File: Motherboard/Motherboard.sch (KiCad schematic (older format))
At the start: 163 parts, among them J1 Jack-DC_18v, J2 65SIB_Connector, J3 DB9_Header, J4 GPIO_Connector, J5 Expansion_Connector, J6 Expansion_Connector, J7 Expansion_Connector, J8 Expansion_Connector, P1 POWER TERMINAL, Q1 2N3055, Q2 TIC106, SW1 SW_DPDT, SW2 FUSE RESET, SW3 PROCESSOR RESET, U1 LM7812_TO220, U13 LM386, U14 LM7912_TO220, U4 LM7805_TO220, X1 ACO-8MHz

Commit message: Completed schematic for 2.3...
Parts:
- added ROM_NOR1, ROM_NOR2 (x3): 74HCT04, symbol 74xx:74HCT04
- gave numbers to parts that had none: 21
- renumbered RAM_NAND to RAM_NAND2, RAM_NOR to RAM_NOR1
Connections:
- net A14: now also ROM_NOR1.9, ROM_NOR2.9, ROM_NOR2.9, ROM_NOR2.9; no longer ROM1_NAND1.10, ROM2_NAND1.10, ROM3_NAND1.10, ROM4_NAND1.10
- net ROM2_EN: now also ROM_NOR1.1, ROM_NOR2.1; no longer ROM_NOR1.9, ROM_NOR2.9
- net ROM3_EN: now also ROM_NOR2.9; no longer ROM_NOR2.1
- net ROM4_EN: now also ROM_NOR3.1; no longer ROM_NOR3.9
- net at ROM2_NAND1.5: now also ROM_NOR1.6; no longer ROM_NOR1.12
- net at ROM2_NAND1.6: now also ROM_NOR1.3; no longer ROM_NOR1.11
- net at ROM2_NAND1.8: now also ROM_NOR1.5; no longer ROM_NOR1.13
- net at ROM2_NAND1.1: now also ROM_NOR1.4; no longer ROM_NOR1.10
- net at ROM2_NAND1.2: now also ROM_NOR1.2; no longer ROM_NOR1.8
- net at ROM2_NAND2.5: now also ROM_NOR2.6; no longer ROM_NOR2.12
- net at ROM2_NAND2.6: now also ROM_NOR2.3; no longer ROM_NOR2.11
- net at ROM2_NAND2.8: now also ROM_NOR2.5; no longer ROM_NOR2.13
- net at ROM2_NAND2.1: now also ROM_NOR2.4; no longer ROM_NOR2.10
- net at ROM2_NAND2.2: now also ROM_NOR2.2; no longer ROM_NOR2.8
- net at ROM3_NAND2.5: now also ROM_NOR2.12; no longer ROM_NOR2.6
- net at ROM3_NAND2.6: now also ROM_NOR2.11; no longer ROM_NOR2.3
- net at ROM3_NAND2.8: now also ROM_NOR2.13; no longer ROM_NOR2.5
- net at ROM3_NAND2.1: now also ROM_NOR2.10; no longer ROM_NOR2.4
- net at ROM3_NAND2.2: now also ROM_NOR2.8; no longer ROM_NOR2.2
- net at ROM4_NAND2.5: now also ROM_NOR3.6; no longer ROM_NOR3.12
- net at ROM4_NAND2.6: now also ROM_NOR3.3; no longer ROM_NOR3.11
- net at ROM4_NAND2.8: now also ROM_NOR3.5; no longer ROM_NOR3.13
- net at ROM4_NAND2.1: now also ROM_NOR3.4; no longer ROM_NOR3.10
- net at ROM4_NAND2.2: now also ROM_NOR3.2; no longer ROM_NOR3.8
- new net: ROM2_NAND1.10, ROM_NOR2.8
- new net: ROM3_NAND1.10, ROM_NOR2.8
- new net: ROM4_NAND1.10, ROM_NOR2.8
- new net: ROM1_NAND1.10, ROM_NOR1.8
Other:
- note added: "Read-Only Memory\nBank 1 high"
- note added: "Read-Only Memory\nBank 2 high"
- note added: "Read-Only Memory\nBank 2 low"
- note added: "Read-Only Memory\nBank 3 low"
- note added: "Read-Only Memory\nBank 4 high"
- note added: "Read-Only Memory\nbank 4 low"
- note removed: "Read-Only Memory\nROM Bank 2"
- note removed: "Read-Only Memory\nROM bank 4 high"
- moved on the sheet: ROM1_NAND1A, ROM1_NAND1B, ROM1_NAND1C, ROM2_NAND1A, ROM2_NAND1B, ROM2_NAND1C, ROM3_NAND1A, ROM3_NAND1B, ROM3_NAND1C, ROM4_NAND1A, ROM4_NAND1B, ROM4_NAND1C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

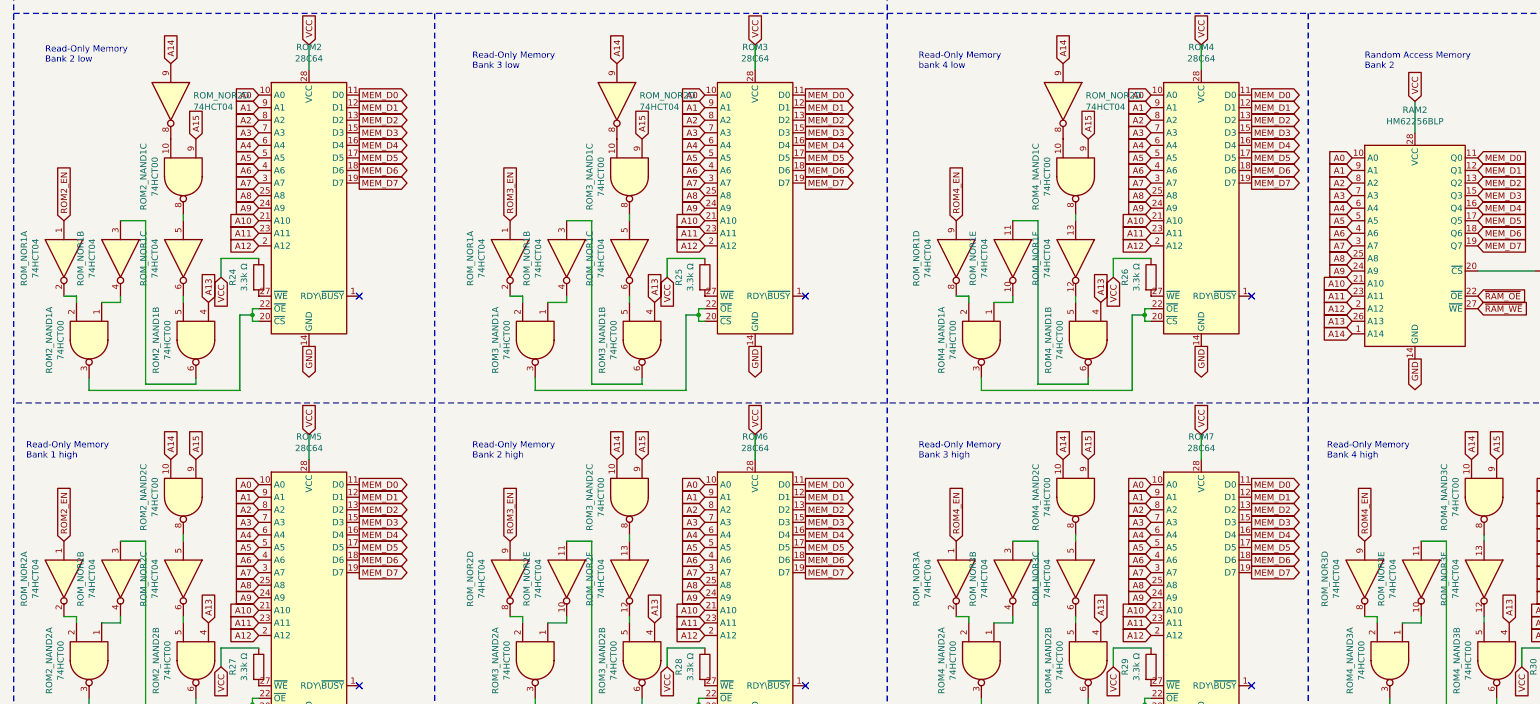
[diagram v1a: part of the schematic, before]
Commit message: Bug fixes...
Multiple components had the same name, this has been corrected.
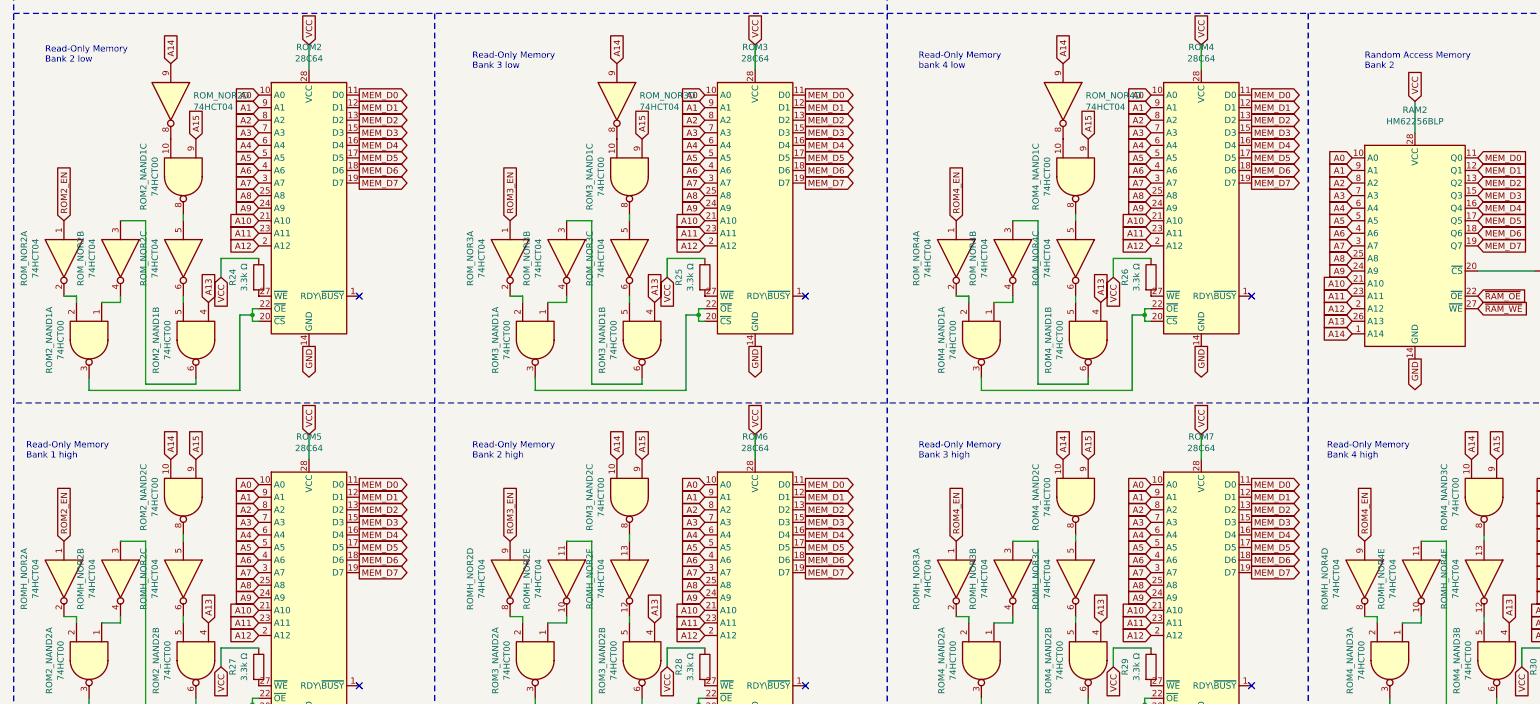
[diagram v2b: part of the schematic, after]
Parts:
- ROMH_NOR3, ROMH_NOR4: renamed from ROM_NOR3; footprint Package_DIP:DIP-14_W7.62mm_Socket_LongPads -> (none)
- ROM_NOR1: footprint Package_DIP:DIP-14_W7.62mm_Socket_LongPads -> (none)
- ROM_NOR2: footprint (none) -> Package_DIP:DIP-14_W7.62mm_Socket_LongPads
- ROM_NOR3, ROM_NOR4: renamed from ROM_NOR1; footprint Package_DIP:DIP-14_W7.62mm_Socket_LongPads -> (none)
- renumbered ROM_NOR2 to ROMH_NOR2, ROM_NOR1 to ROM_NOR2, ROM_NOR2 to ROM_NOR3, ROM_NOR2 to ROM_NOR4
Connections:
- net ROM4_EN: now also ROM_NOR4.1; no longer ROM_NOR4.9
- net at ROM4_NAND1.5: now also ROM_NOR4.6; no longer ROM_NOR4.12
- net at ROM4_NAND1.6: now also ROM_NOR4.3; no longer ROM_NOR4.11
- net at ROM4_NAND1.8: now also ROM_NOR4.5; no longer ROM_NOR4.13
- net at ROM4_NAND1.1: now also ROM_NOR4.4; no longer ROM_NOR4.10
- net at ROM4_NAND1.2: now also ROM_NOR4.2; no longer ROM_NOR4.8

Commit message: Bug fixes and added some traces...
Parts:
- removed CS_ROM_NAND1, ROM1_NAND1, ROM2_NAND1, ROM2_NAND2, ROM3_NAND1, ROM3_NAND2, ROM4_NAND1, ROM4_NAND2, ROM4_NAND3: 74HCT00, Package_DIP:DIP-14_W7.62mm_Socket_LongPads, symbol 74xx:74HCT00
- removed CS_ROM_NOR1, ROMH_NOR2: 74HCT04, Package_DIP:DIP-14_W7.62mm_Socket_LongPads, symbol 74xx:74HCT04
- removed ROMH_NOR3, ROMH_NOR4: 74HCT04, symbol 74xx:74HCT04
- removed unit 4 of ROM_NOR1
- removed unit 3 of ROM_NOR1
- removed unit 2 of ROM_NOR1
- removed unit 3 of ROM_NOR2
- removed unit 2 of ROM_NOR2
- removed unit 1 of ROM_NOR2
- removed unit 3 of ROM_NOR3
- removed unit 2 of ROM_NOR3
- removed unit 1 of ROM_NOR3
- removed unit 3 of ROM_NOR4
- removed unit 2 of ROM_NOR4
- removed unit 1 of ROM_NOR4
- added FUSE_DISABLE1: Jumper_2_Open, Connector_PinHeader_2.54mm:PinHeader_1x02_P2.54mm_Vertical, symbol Jumper:Jumper_2_Open
- added ROM1_NAND4, ROM2_NAND4, ROM3_NAND4, ROM4_NAND4, SHARED_ROM2: 74LS20, Package_DIP:DIP-14_W7.62mm_Socket_LongPads, symbol 74xx:74LS20
- ROM_NOR1: footprint (none) -> Package_DIP:DIP-14_W7.62mm_Socket_LongPads
- ROM_NOR1: renamed from ROM_NOR3; footprint (none) -> Package_DIP:DIP-14_W7.62mm_Socket_LongPads
- ROM_NOR1: renamed from ROM_NOR4; footprint (none) -> Package_DIP:DIP-14_W7.62mm_Socket_LongPads
- renumbered CS_65SIB_NOR2 to CS_65SIB_NOR1, ROM5 to ROM1H1, ROM1 to ROM1L1, ROM6 to ROM2H1, ROM2 to ROM2L1, ROM7 to ROM3H1, ROM3 to ROM3L1, ROM8 to ROM4H1, ROM4 to ROM4L1, ROM_NOR2 to ROM_NOR1
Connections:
- net A10: now also CS_65SIB_NOR1.11; no longer CS_65SIB_NOR1.13
- net A11: now also CS_65SIB_NOR1.13; no longer CS_65SIB_NOR1.1
- net A13: now also ROM1_NAND4.1, ROM1_NAND4.9, ROM2_NAND4.1, ROM2_NAND4.9, ROM3_NAND4.1, ROM3_NAND4.9, ROM4_NAND4.1, ROM4_NAND4.9, SHARED_ROM2.1, SHARED_ROM2.2
- net A14: now also ROM_NOR1.1, ROM_NOR1.3, ROM_NOR1.5, ROM1_NAND4.10, ROM2_NAND4.10, ROM3_NAND4.10, ROM4_NAND4.10, SHARED_ROM2.4; no longer ROM_NOR1.9, ROM_NOR1.9
- net A15: now also ROM1_NAND4.12, ROM1_NAND4.4, ROM2_NAND4.12, ROM2_NAND4.4, ROM3_NAND4.12, ROM3_NAND4.4, ROM4_NAND4.12, ROM4_NAND4.4, SHARED_ROM2.5
- net A8: now also CS_65SIB_NOR1.5; no longer CS_65SIB_NOR1.9
- net A9: now also CS_65SIB_NOR1.9; no longer CS_65SIB_NOR1.11
- net FUSE_IN: now also FUSE_DISABLE1.1 (A)
- net FUSE_OUT: now also FUSE_DISABLE1.2 (B)
- net ROM1_EN: now also ROM1_NAND4.13, ROM1_NAND4.5; no longer ROM_NOR1.1
- net ROM2_EN: now also ROM2_NAND4.13, ROM2_NAND4.5
- net ROM3_EN: now also ROM3_NAND4.13, ROM3_NAND4.5
- net ROM4_EN: now also ROM4_NAND4.13, ROM4_NAND4.5
- net at SHARED_ROM1.20 (~CS), SHARED_ROM1.22 (~OE): now also SHARED_ROM2.6
- net at CS_65SIB_AND4.1: now also CS_65SIB_NOR1.6; no longer CS_65SIB_NOR1.8
- net at CS_65SIB_AND4.2: now also CS_65SIB_NOR1.8; no longer CS_65SIB_NOR1.10
- net at CS_65SIB_AND4.4: now also CS_65SIB_NOR1.10; no longer CS_65SIB_NOR1.12
- net at CS_65SIB_AND4.5: now also CS_65SIB_NOR1.12; no longer CS_65SIB_NOR1.2
- net at ROM2L1.20 (~CS), ROM2L1.22 (~OE): now also ROM2_NAND4.6
- net at ROM3L1.20 (~CS), ROM3L1.22 (~OE): now also ROM3_NAND4.6
- net at ROM4L1.20 (~CS), ROM4L1.22 (~OE): now also ROM4_NAND4.6
- net at ROM_NOR1.8: now also ROM4_NAND4.2
- net at ROM1H1.20 (~CS), ROM1H1.22 (~OE): now also ROM1_NAND4.8
- net at ROM2H1.20 (~CS), ROM2H1.22 (~OE): now also ROM2_NAND4.8
- net at ROM3H1.20 (~CS), ROM3H1.22 (~OE): now also ROM3_NAND4.8
- net at ROM4H1.20 (~CS), ROM4H1.22 (~OE): now also ROM4_NAND4.8
- net at ROM1L1.20 (~CS), ROM1L1.22 (~OE): now also ROM1_NAND4.6
- net at ROM_NOR1.2: now also ROM1_NAND4.2
- new net: ROM2_NAND4.2, ROM_NOR1.4
- new net: ROM3_NAND4.2, ROM_NOR1.6
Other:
- note removed: "Address space: 0xD014 - 0xD017"
- note removed: "IRQ0"
- moved on the sheet: ROM_NOR1D

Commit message: 525 traces to go...
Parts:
- added H1, H2, H3, H4, H5, H6: MountingHole, MountingHole:MountingHole_3.2mm_M3, symbol Mechanical:MountingHole
- J2: footprint Connector_PinHeader_2.54mm:PinHeader_2x10_P2.54mm_Vertical -> Connector_IDC:IDC-Header_2x10-1MP_P2.54mm_Latch6.5mm_Vertical
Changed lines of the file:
@@
 L Graphic:Logo_Open_Hardware_Large #LOGO1
 U 1 1 61C12325
-P 8150 22200
-F 0 "#LOGO1" H 8150 22700 50  0001 C CNN
-F 1 "Logo_Open_Hardware_Large" H 8150 21800 50  0001 C CNN
-F 2 "Symbol:OSHW-Logo2_14.6x12mm_SilkScreen" H 8150 22200 50  0001 C CNN
-F 3 "~" H 8150 22200 50  0001 C CNN
-	1    8150 22200
+P 14850 20600
+F 0 "#LOGO1" H 14850 21100 50  0001 C CNN
+F 1 "Logo_Open_Hardware_Large" H 14850 20200 50  0001 C CNN
+F 2 "Symbol:OSHW-Logo2_14.6x12mm_SilkScreen" H 14850 20600 50  0001 C CNN
+F 3 "~" H 14850 20600 50  0001 C CNN
+	1    14850 20600
 	1    0    0    -1
 $EndComp
@@
 F 0 "J2" H 29050 9817 50  0000 C CNN
 F 1 "65SIB_Connector" H 29050 9726 50  0000 C CNN
-F 2 "Connector_PinHeader_2.54mm:PinHeader_2x10_P2.54mm_Vertical" H 29000 9200 50  0001 C CNN
+F 2 "Connector_IDC:IDC-Header_2x10-1MP_P2.54mm_Latch6.5mm_Vertical" H 29000 9200 50  0001 C CNN
 F 3 "~" H 29000 9200 50  0001 C CNN
 	1    29000 9200
@@
 L Graphic:SYM_ESD_Large #SYM2
 U 1 1 62084D56
-P 6950 22300
-F 0 "#SYM2" H 6950 22500 50  0001 C CNN
-F 1 "SYM_ESD_Large" H 6950 22050 50  0001 C CNN
-F 2 "Symbol:ESD-Logo_13.2x12mm_SilkScreen" H 6945 22270 50  0001 C CNN
-F 3 "~" H 6945 22270 50  0001 C CNN
-	1    6950 22300
+P 13650 20700
+F 0 "#SYM2" H 13650 20900 50  0001 C CNN
+F 1 "SYM_ESD_Large" H 13650 20450 50  0001 C CNN
+F 2 "Symbol:ESD-Logo_13.2x12mm_SilkScreen" H 13645 20670 50  0001 C CNN
+F 3 "~" H 13645 20670 50  0001 C CNN
+	1    13650 20700
 	1    0    0    -1
 $EndComp
@@
 L Graphic:SYM_Flash_XLarge #SYM4
 U 1 1 620873CC
-P 6500 22350
-F 0 "#SYM4" V 6350 22350 50  0001 C CNN
-F 1 "SYM_Flash_XLarge" V 6650 22350 50  0001 C CNN
-F 2 "" H 6500 22325 50  0001 C CNN
-F 3 "~" H 6900 22250 50  0001 C CNN
-	1    6500 22350
+P 13200 20750
+F 0 "#SYM4" V 13050 20750 50  0001 C CNN
+F 1 "SYM_Flash_XLarge" V 13350 20750 50  0001 C CNN
+F 2 "Symbol:Symbol_HighVoltage_Type2_CopperTop_Big" H 13200 20725 50  0001 C CNN
+F 3 "~" H 13600 20650 50  0001 C CNN
+	1    13200 20750
 	1    0    0    -1
 $EndComp
@@
 L Graphic:SYM_Hot_Large #SYM3
 U 1 1 620C2A36
-P 7450 22300
-F 0 "#SYM3" H 7450 22500 50  0001 C CNN
-F 1 "SYM_Hot_Large" H 7450 22050 50  0001 C CNN
-F 2 "" H 7450 22100 50  0001 C CNN
-F 3 "~" H 7480 22100 50  0001 C CNN
-	1    7450 22300
+P 14150 20700
+F 0 "#SYM3" H 14150 20900 50  0001 C CNN
+F 1 "SYM_Hot_Large" H 14150 20450 50  0001 C CNN
+F 2 "" H 14150 20500 50  0001 C CNN
+F 3 "~" H 14180 20500 50  0001 C CNN
+	1    14150 20700
 	1    0    0    -1
 $EndComp
@@
 Wire Wire Line
 	5450 2600 5700 2600
-Text Notes 2700 21700 2    50   ~ 0
+Text Notes 2700 20150 2    50   ~ 0
 Miscellaneous parts
 $Comp
@@
 Wire Wire Line
 	7450 6700 7500 6700
-Wire Notes Line
-	1800 22800 8750 22800
-Wire Notes Line
-	1800 21600 8750 21600
 Wire Wire Line
 	13150 5000 12850 5000
@@
 Wire Notes Line
 	19100 1150 19100 16850
-Wire Notes Line
-	8750 21600 8750 22800
-Wire Notes Line
-	1800 21600 1800 22800
 Text GLabel 30150 12700 2    50   Output ~ 0
 ~IRQ3
@@
 	11250 17100 11250 17300
 Wire Notes Line
-	1800 1150 1800 19950
-Wire Notes Line
 	5150 13750 5150 19950
 Wire Notes Line
@@
 	14500 17100 14500 17300
 Wire Notes Line
-	15550 13750 15550 19950
-Wire Notes Line
 	1800 19950 15550 19950
 Wire Wire Line
@@
 Text GLabel 16200 4500 1    50   Input ~ 0
 A13
+Wire Notes Line
+	1800 1150 1800 22800
+Wire Notes Line
+	1800 22800 15550 22800
+Wire Notes Line
+	15550 13750 15550 22800
+$Comp
+L Mechanical:MountingHole H2
+U 1 1 6483DDE7
+P 14650 21150
+F 0 "H2" H 14750 21196 50  0000 L CNN
+F 1 "MountingHole" H 14750 21105 50  0000 L CNN
+F 2 "MountingHole:MountingHole_3.2mm_M3" H 14650 21150 50  0001 C CNN
+F 3 "~" H 14650 21150 50  0001 C CNN
+	1    14650 21150
+	1    0    0    -1
+$EndComp
+$Comp
+L Mechanical:MountingHole H1
+U 1 1 6483E48F
+P 13900 21150
+F 0 "H1" H 14000 21196 50  0000 L CNN
+F 1 "MountingHole" H 14000 21105 50  0000 L CNN
+F 2 "MountingHole:MountingHole_3.2mm_M3" H 13900 21150 50  0001 C CNN
+F 3 "~" H 13900 21150 50  0001 C CNN
+	1    13900 21150
+	1    0    0    -1
+$EndComp
+$Comp
+L Mechanical:MountingHole H4
+U 1 1 6483EC45
+P 14650 21400
+F 0 "H4" H 14750 21446 50  0000 L CNN
+F 1 "MountingHole" H 14750 21355 50  0000 L CNN
+F 2 "MountingHole:MountingHole_3.2mm_M3" H 14650 21400 50  0001 C CNN
+F 3 "~" H 14650 21400 50  0001 C CNN
+	1    14650 21400
+	1    0    0    -1
+$EndComp
+$Comp
+L Mechanical:MountingHole H3
+U 1 1 6483EC4B
+P 13900 21400
+F 0 "H3" H 14000 21446 50  0000 L CNN
+F 1 "MountingHole" H 14000 21355 50  0000 L CNN
+F 2 "MountingHole:MountingHole_3.2mm_M3" H 13900 21400 50  0001 C CNN
+F 3 "~" H 13900 21400 50  0001 C CNN
+	1    13900 21400
+	1    0    0    -1
+$EndComp
+$Comp
+L Mechanical:MountingHole H6
+U 1 1 6489366B
+P 14650 21650
+F 0 "H6" H 14750 21696 50  0000 L CNN
+F 1 "MountingHole" H 14750 21605 50  0000 L CNN
+F 2 "MountingHole:MountingHole_3.2mm_M3" H 14650 21650 50  0001 C CNN
+F 3 "~" H 14650 21650 50  0001 C CNN
+	1    14650 21650
+	1    0    0    -1
+$EndComp
+$Comp
+L Mechanical:MountingHole H5
+U 1 1 64893671
+P 13900 21650
+F 0 "H5" H 14000 21696 50  0000 L CNN
+F 1 "MountingHole" H 14000 21605 50  0000 L CNN
+F 2 "MountingHole:MountingHole_3.2mm_M3" H 13900 21650 50  0001 C CNN
+F 3 "~" H 13900 21650 50  0001 C CNN
+	1    13900 21650
+	1    0    0    -1
+$EndComp
 $EndSCHEMATC
